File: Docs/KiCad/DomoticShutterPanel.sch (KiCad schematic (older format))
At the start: 32 parts, among them J1 Conn_01x02, J2 3.3V DC-DC Step-Down Power Mo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, J3 Conn_01x04, J4 BOOT OPTION, J5 UART COM, J6 Conn_01x04, J7 Conn_01x03, J9 Conn_01x03, K1 SRD-05VDC-SL-C, SW1 SW_Push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

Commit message: Updated 3D model to Crossed layout
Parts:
- added R? (x2): 8.2k, symbol CustomLibraries_Device:R
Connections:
- wire segments 144 -> 154
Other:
- note added: "ESP-WROOM-02"
- note added: "I2C PULLUP RESISTOR"
- note removed: "ESP-13e"
- moved on the sheet: J3, J?
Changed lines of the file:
@@
 Wire Wire Line
 	2400 1200 2950 1200
-Text Notes 8750 2200 0    50   ~ 0
+Text Notes 8350 2550 0    50   ~ 0
 LCD 16x2 I2C
 $Comp
 L CustomLibraries_connectors:Conn_01x04 J3
 U 1 1 5EA32128
-P 9350 2500
-F 0 "J3" H 9430 2492 50  0000 L CNN
-F 1 "Conn_01x04" H 9430 2401 50  0000 L CNN
-F 2 "Connector_PinHeader_2.54mm:PinHeader_1x04_P2.54mm_Vertical" H 9350 2500 50  0001 C CNN
-F 3 "~" H 9350 2500 50  0001 C CNN
-	1    9350 2500
-	1    0    0    -1
-$EndComp
-Wire Wire Line
-	9150 2400 9050 2400
-Wire Wire Line
-	9150 2500 8900 2500
-Wire Wire Line
-	9150 2600 8900 2600
-Wire Wire Line
-	9150 2700 8900 2700
+P 8950 2850
+F 0 "J3" H 9030 2842 50  0000 L CNN
+F 1 "Conn_01x04" H 9030 2751 50  0000 L CNN
+F 2 "Connector_PinHeader_2.54mm:PinHeader_1x04_P2.54mm_Vertical" H 8950 2850 50  0001 C CNN
+F 3 "~" H 8950 2850 50  0001 C CNN
+	1    8950 2850
+	1    0    0    -1
+$EndComp
+Wire Wire Line
+	8750 2750 8650 2750
+Wire Wire Line
+	8750 2850 8500 2850
+Wire Wire Line
+	8750 2950 8500 2950
+Wire Wire Line
+	8750 3050 8500 3050
 $Comp
 L CustomLibraries_power:GND #PWR04
 U 1 1 5EA49EAB
-P 9050 2850
-F 0 "#PWR04" H 9050 2600 50  0001 C CNN
-F 1 "GND" H 9055 2677 50  0000 C CNN
-F 2 "" H 9050 2850 50  0001 C CNN
-F 3 "" H 9050 2850 50  0001 C CNN
-	1    9050 2850
-	1    0    0    -1
-$EndComp
-Wire Wire Line
-	8900 2500 8900 2450
-Text Label 8950 2700 0    39   ~ 0
+P 8650 3200
+F 0 "#PWR04" H 8650 2950 50  0001 C CNN
+F 1 "GND" H 8655 3027 50  0000 C CNN
+F 2 "" H 8650 3200 50  0001 C CNN
+F 3 "" H 8650 3200 50  0001 C CNN
+	1    8650 3200
+	1    0    0    -1
+$EndComp
+Wire Wire Line
+	8500 2850 8500 2800
+Text Label 8550 3050 0    39   ~ 0
 I2C_SCL
 Wire Notes Line
-	8700 2100 9900 2100
-Wire Notes Line
-	9900 3100 8700 3100
-Wire Notes Line
-	9900 2100 9900 3100
-Wire Notes Line
-	8700 2100 8700 3100
+	8300 2450 9500 2450
+Wire Notes Line
+	9500 3450 8300 3450
+Wire Notes Line
+	9500 2450 9500 3450
+Wire Notes Line
+	8300 2450 8300 3450
 $Comp
 L CustomLibraries_SRD-05VDC-SL-C:SRD-05VDC-SL-C K1
@@
 L CustomLibraries_power:+5V #PWR0101
 U 1 1 5EB0B1CD
-P 8900 2450
-F 0 "#PWR0101" H 8900 2300 50  0001 C CNN
-F 1 "+5V" H 8915 2623 50  0000 C CNN
-F 2 "" H 8900 2450 50  0001 C CNN
-F 3 "" H 8900 2450 50  0001 C CNN
-	1    8900 2450
-	1    0    0    -1
-$EndComp
-Wire Wire Line
-	9050 2400 9050 2850
+P 8500 2800
+F 0 "#PWR0101" H 8500 2650 50  0001 C CNN
+F 1 "+5V" H 8515 2973 50  0000 C CNN
+F 2 "" H 8500 2800 50  0001 C CNN
+F 3 "" H 8500 2800 50  0001 C CNN
+	1    8500 2800
+	1    0    0    -1
+$EndComp
+Wire Wire Line
+	8650 2750 8650 3200
 $Comp
 L CustomLibraries_power:+5V #PWR0102
@@
 	1    0    0    -1
 $EndComp
-Text Notes 5150 4050 0    60   ~ 0
-ESP-13e
+Text Notes 4300 4050 0    60   ~ 0
+ESP-WROOM-02
 Wire Notes Line
 	3950 6850 3950 3900
@@
 Text Label 3050 6650 3    60   ~ 0
 A7
-Wire Notes Line
-	1875 4100 3050 4100
 Text Label 3600 5450 0    60   ~ 0
 A3
@@
 Wire Wire Line
 	5900 5800 6050 5800
-Text Label 8950 2600 0    39   ~ 0
+Text Label 8550 2950 0    39   ~ 0
 I2C_SDA
 Wire Wire Line
@@
 L CustomLibraries_connectors:Conn_01x03 J?
 U 1 1 5F3D7AAB
-P 9250 1100
-F 0 "J?" H 9330 1142 50  0000 L CNN
-F 1 "Conn_01x03" H 9330 1051 50  0000 L CNN
-F 2 "Connector_PinHeader_2.54mm:PinHeader_1x03_P2.54mm_Vertical" H 9250 1100 50  0001 C CNN
-F 3 "~" H 9250 1100 50  0001 C CNN
-	1    9250 1100
-	1    0    0    -1
-$EndComp
-Wire Notes Line
-	8750 1550 9900 1550
-Wire Notes Line
-	9900 1550 9900 600
-Wire Notes Line
-	9900 600  8750 600
-Wire Notes Line
-	8750 600  8750 1550
-Text Notes 8800 700  0    39   ~ 0
+P 8950 2050
+F 0 "J?" H 9030 2092 50  0000 L CNN
+F 1 "Conn_01x03" H 9030 2001 50  0000 L CNN
+F 2 "Connector_PinHeader_2.54mm:PinHeader_1x03_P2.54mm_Vertical" H 8950 2050 50  0001 C CNN
+F 3 "~" H 8950 2050 50  0001 C CNN
+	1    8950 2050
+	1    0    0    -1
+$EndComp
+Text Notes 8350 1700 0    39   ~ 0
 Lamp button
 Wire Wire Line
@@
 Wire Wire Line
 	8850 4600 8850 4500
+$Comp
+L CustomLibraries_power:+3V3 #PWR?
+U 1 1 5F493D6E
+P 10000 2700
+F 0 "#PWR?" H 10000 2550 50  0001 C CNN
+F 1 "+3V3" H 10015 2873 50  0000 C CNN
+F 2 "" H 10000 2700 50  0001 C CNN
+F 3 "" H 10000 2700 50  0001 C CNN
+	1    10000 2700
+	1    0    0    -1
+$EndComp
+Text Label 10150 3200 0    39   ~ 0
+I2C_SCL
+Text Label 10150 3300 0    39   ~ 0
+I2C_SDA
+Text Notes 9700 2450 0    39   ~ 0
+I2C PULLUP RESISTOR
+Wire Notes Line
+	8300 2400 9500 2400
+Wire Notes Line
+	8300 2400 8300 1600
+Wire Notes Line
+	8300 1600 9500 1600
+Wire Notes Line
+	9500 1600 9500 2400
+$Comp
+L CustomLibraries_Device:R R?
+U 1 1 5F4B85F8
+P 10100 2950
+F 0 "R?" H 10170 2996 50  0000 L CNN
+F 1 "8.2k" H 10170 2905 50  0000 L CNN
+F 2 "" V 10030 2950 50  0001 C CNN
+F 3 "~" H 10100 2950 50  0001 C CNN
+	1    10100 2950
+	1    0    0    -1
+$EndComp
+$Comp
+L CustomLibraries_Device:R R?
+U 1 1 5F4B940D
+P 9900 2950
+F 0 "R?" H 9700 3000 50  0000 L CNN
+F 1 "8.2k" H 9650 2900 50  0000 L CNN
+F 2 "" V 9830 2950 50  0001 C CNN
+F 3 "~" H 9900 2950 50  0001 C CNN
+	1    9900 2950
+	1    0    0    -1
+$EndComp
+Wire Notes Line
+	9600 3450 10450 3450
+Wire Notes Line
+	9600 2300 10450 2300
+Wire Notes Line
+	10450 2300 10450 3450
+Wire Notes Line
+	9600 2300 9600 3450
+Wire Wire Line
+	9900 3100 9900 3200
+Connection ~ 9900 3200
+Wire Wire Line
+	9900 3200 10400 3200
+Wire Wire Line
+	10100 3100 10100 3300
+Connection ~ 10100 3300
+Wire Wire Line
+	10100 3300 10400 3300
+Wire Wire Line
+	9900 2800 9900 2700
+Wire Wire Line
+	9900 2700 10000 2700
+Wire Wire Line
+	10100 2800 10100 2700
+Wire Wire Line
+	10100 2700 10000 2700
+Connection ~ 10000 2700
+Wire Wire Line
+	9700 3200 9900 3200
+Wire Wire Line
+	9700 3300 10100 3300
 $EndSCHEMATC

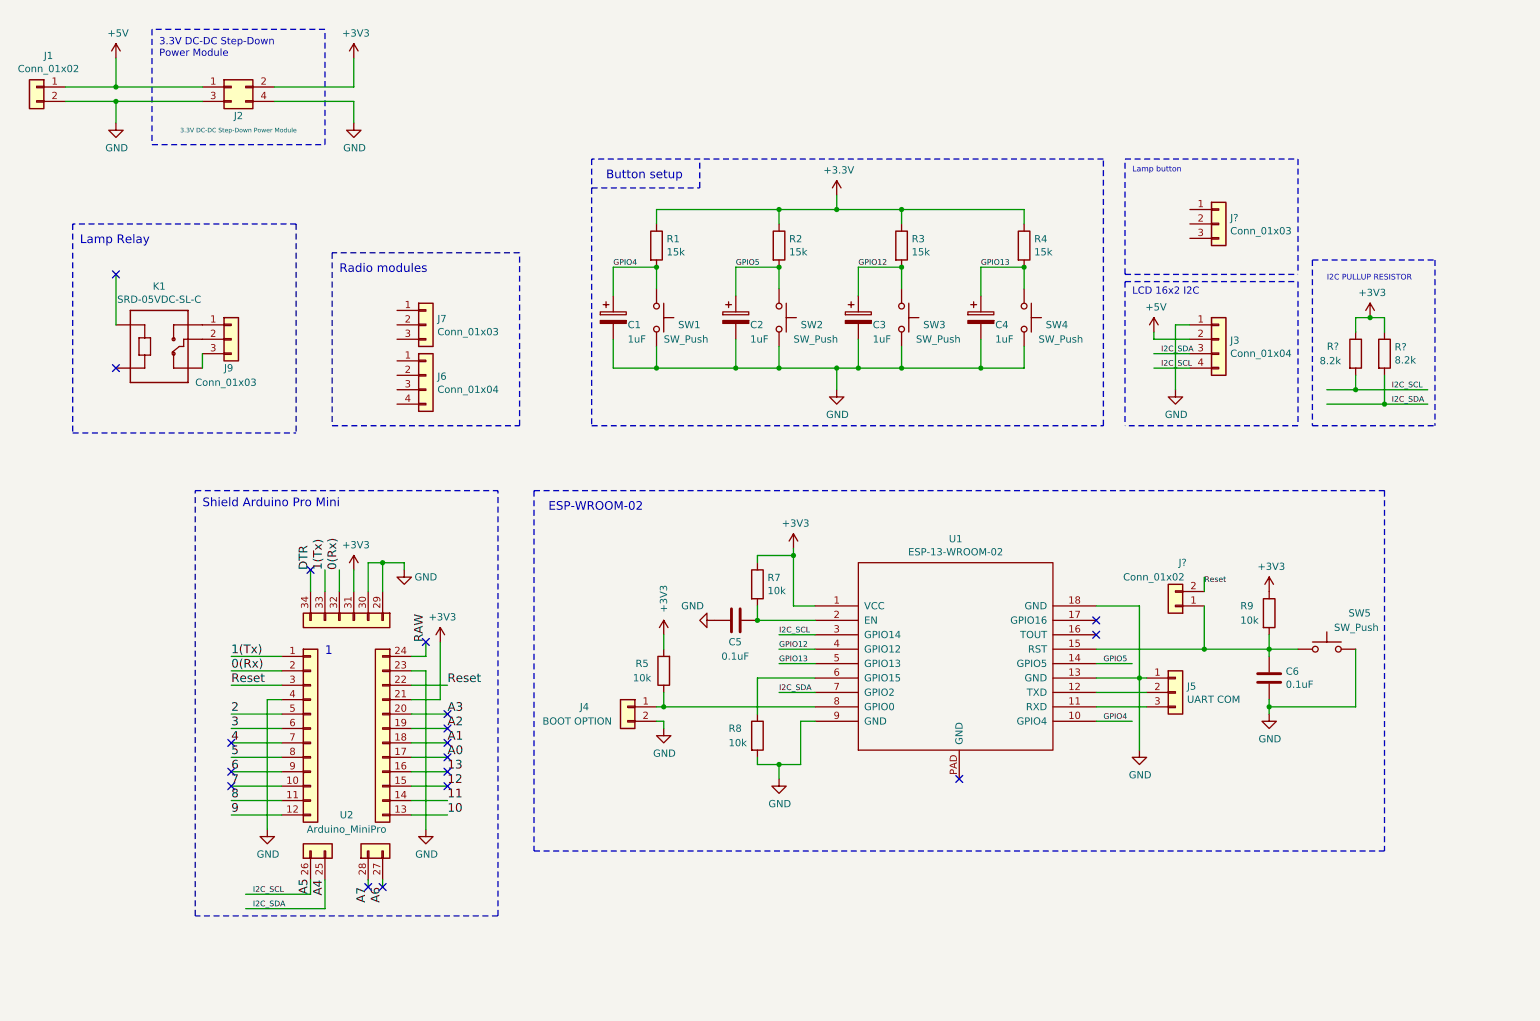
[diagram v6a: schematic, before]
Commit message: Changed text labels
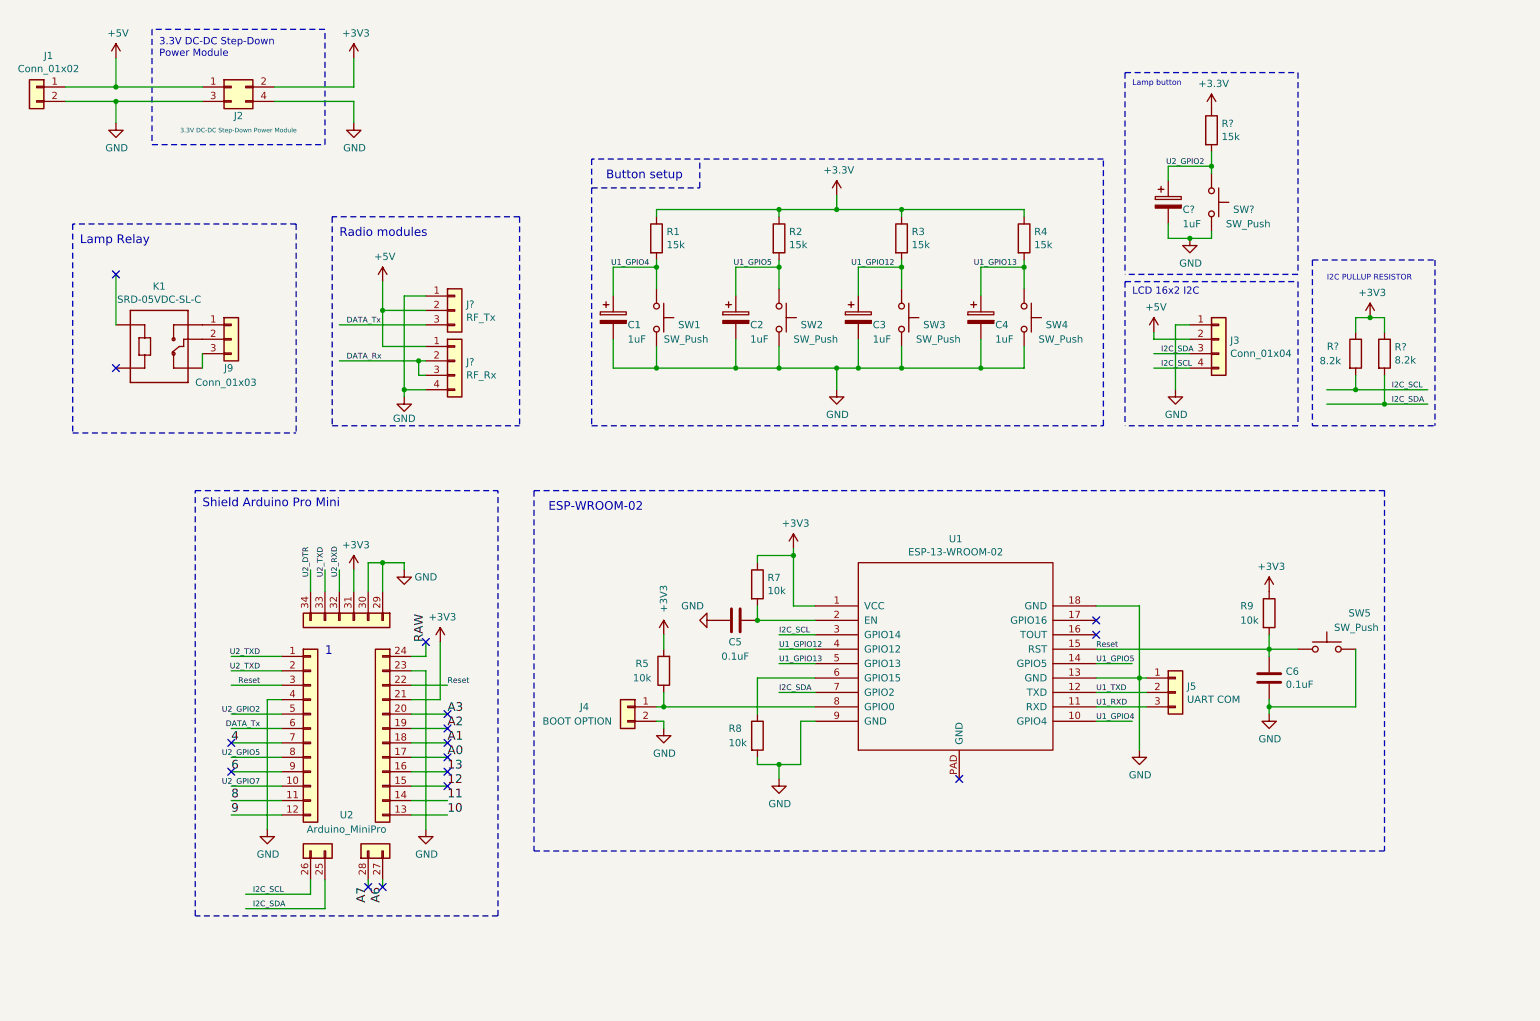
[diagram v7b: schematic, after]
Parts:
- removed J?: Conn_01x03, Connector_PinHeader_2.54mm:PinHeader_1x03_P2.54mm_Vertical, symbol CustomLibraries_connectors:Conn_01x03
- removed J?: Conn_01x02, symbol CustomLibraries_connectors:Conn_01x02
- added C?: 1uF, Capacitor_THT:C_Radial_D5.0mm_H5.0mm_P2.00mm, symbol CustomLibraries_Device:CP
- added R?: 15k, Resistor_THT:R_Axial_DIN0204_L3.6mm_D1.6mm_P1.90mm_Vertical, symbol CustomLibraries_Device:R
- added SW?: SW_Push, Custom_libraries:SW_PUSH_6mm, symbol CustomLibraries_Switch:SW_Push
- J?: renamed from J6; value Conn_01x04 -> RF_Rx
- J?: renamed from J7; value Conn_01x03 -> RF_Tx
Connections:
- net labels added: DATA_Rx, DATA_Tx, U1_GPIO12, U1_GPIO13, U1_GPIO4, U1_GPIO5, U1_RXD, U1_TXD, U2_DTR, U2_GPIO2, U2_GPIO5, U2_GPIO7, U2_RXD, U2_TXD
- net labels removed: 0(Rx), 1(Tx), 2, 3, 5, 7, A4, A5, DTR, GPIO12, GPIO13, GPIO4, GPIO5
- wire segments 154 -> 176
- no-connect marks 18 -> 16
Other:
- moved on the sheet: J?, R1, R2, R3, R4

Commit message: Added buzzer and 3d model updated
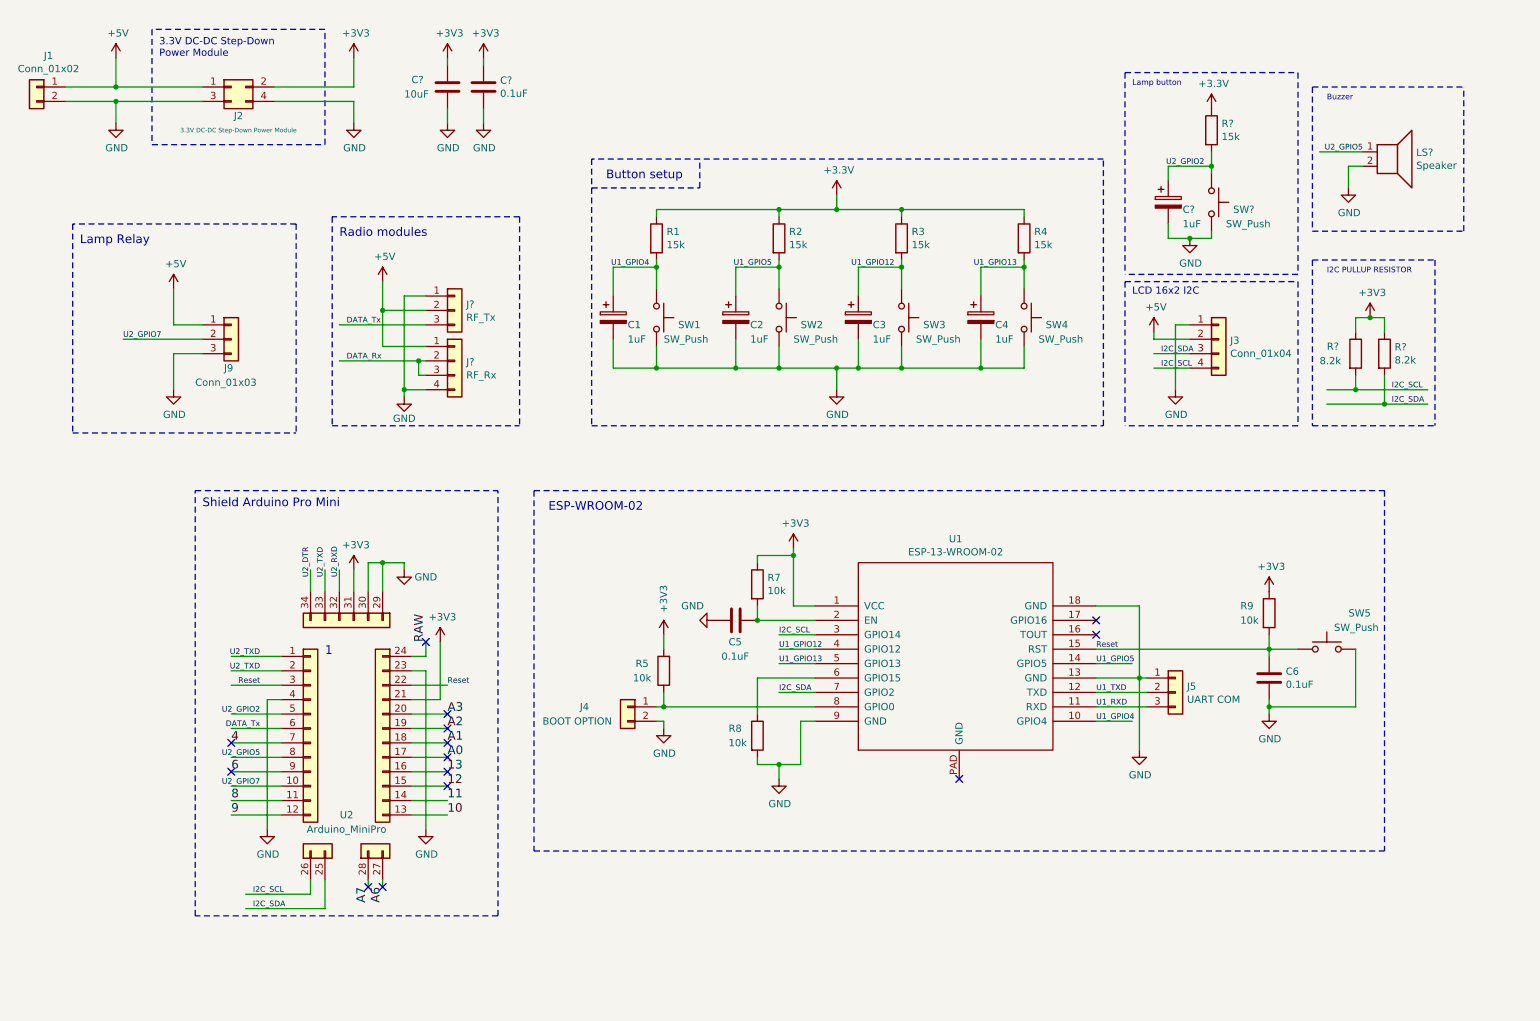
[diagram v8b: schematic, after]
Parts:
- removed K1: SRD-05VDC-SL-C, Custom_libraries:RELAY_SRD-05VDC-SL-C, symbol CustomLibraries_SRD-05VDC-SL-C:SRD-05VDC-SL-C
- added C?: 10uF, symbol CustomLibraries_Device:C
- added C?: 0.1uF, symbol CustomLibraries_Device:C
- added LS?: Speaker, symbol CustomLibraries_Device:Speaker
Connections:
- wire segments 176 -> 186
- no-connect marks 16 -> 14
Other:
- note added: "Buzzer"
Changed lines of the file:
@@
 Sheet 1 1
 Title "Roller Shutter Controller Panel"
-Date "2020-04-24"
+Date "2020-08-30"
 Rev ""
 Comp ""
@@
 Wire Wire Line
 	6300 1950 6750 1950
-Wire Wire Line
-	1300 2400 1300 2750
-Wire Wire Line
-	1900 2950 1900 3050
-$Comp
-L CustomLibraries_connectors:Conn_01x03 J9
-U 1 1 5EACF56F
-P 2100 2850
-F 0 "J9" H 2050 2650 50  0000 L CNN
-F 1 "Conn_01x03" H 1850 2550 50  0000 L CNN
-F 2 "Connector_PinHeader_2.54mm:PinHeader_1x03_P2.54mm_Vertical" H 2100 2850 50  0001 C CNN
-F 3 "~" H 2100 2850 50  0001 C CNN
-	1    2100 2850
-	1    0    0    -1
-$EndComp
-Wire Notes Line
-	1000 3500 2550 3500
-Wire Notes Line
-	2550 2050 1000 2050
-Text Notes 1050 2200 0    60   ~ 0
-Lamp Relay
-Wire Notes Line
-	1000 2050 1000 3500
-Wire Notes Line
-	2550 2050 2550 3500
 $Comp
 L CustomLibraries_connectors:Conn_01x02 J1
@@
 Wire Notes Line
 	8300 2450 8300 3450
-$Comp
-L CustomLibraries_SRD-05VDC-SL-C:SRD-05VDC-SL-C K1
-U 1 1 5EACF577
-P 1600 2850
-F 0 "K1" H 1600 3217 50  0000 C CNN
-F 1 "SRD-05VDC-SL-C" H 1600 3126 50  0000 C CNN
-F 2 "Custom_libraries:RELAY_SRD-05VDC-SL-C" H 1600 2850 50  0001 L BNN
-F 3 "" H 1600 2850 50  0001 L BNN
-F 4 "IPC-7251" H 1600 2850 50  0001 L BNN "Campo4"
-	1    1600 2850
-	1    0    0    -1
-$EndComp
-NoConn ~ 1300 3050
-NoConn ~ 1300 2400
 $Comp
 L CustomLibraries_power:+5V #PWR0101
@@
 Text Label 10150 3300 0    39   ~ 0
 I2C_SDA
-Text Notes 9700 2450 0    39   ~ 0
+Text Notes 9700 2400 0    39   ~ 0
 I2C PULLUP RESISTOR
 $Comp
@@
 Text Label 2650 4500 1    39   ~ 0
 U2_DTR
+$Comp
+L CustomLibraries_Device:Speaker LS?
+U 1 1 5F4B04D1
+P 10150 1550
+F 0 "LS?" H 10320 1546 50  0000 L CNN
+F 1 "Speaker" H 10320 1455 50  0000 L CNN
+F 2 "" H 10150 1350 50  0001 C CNN
+F 3 "~" H 10140 1500 50  0001 C CNN
+	1    10150 1550
+	1    0    0    -1
+$EndComp
+Wire Wire Line
+	9950 1650 9850 1650
+Wire Wire Line
+	9850 1650 9850 1800
+Wire Wire Line
+	9950 1550 9650 1550
+Text Label 9950 1550 2    39   ~ 0
+U2_GPIO5
+$Comp
+L CustomLibraries_power:GND #PWR?
+U 1 1 5F4C460A
+P 9850 1800
+F 0 "#PWR?" H 9850 1550 50  0001 C CNN
+F 1 "GND" H 9855 1627 50  0000 C CNN
+F 2 "" H 9850 1800 50  0001 C CNN
+F 3 "" H 9850 1800 50  0001 C CNN
+	1    9850 1800
+	1    0    0    -1
+$EndComp
+Wire Notes Line
+	9600 1100 9600 2100
+Wire Notes Line
+	9600 2100 10650 2100
+Wire Notes Line
+	10650 2100 10650 1100
+Wire Notes Line
+	9600 1100 10650 1100
+Text Notes 9700 1200 0    39   ~ 0
+Buzzer
+Wire Wire Line
+	3600 900  3600 950
+$Comp
+L CustomLibraries_power:GND #PWR?
+U 1 1 5F4B3969
+P 3600 1350
+F 0 "#PWR?" H 3600 1100 50  0001 C CNN
+F 1 "GND" H 3605 1177 50  0000 C CNN
+F 2 "" H 3600 1350 50  0001 C CNN
+F 3 "" H 3600 1350 50  0001 C CNN
+	1    3600 1350
+	1    0    0    -1
+$EndComp
+$Comp
+L CustomLibraries_power:+3V3 #PWR?
+U 1 1 5F4B3972
+P 3600 900
+F 0 "#PWR?" H 3600 750 50  0001 C CNN
+F 1 "+3V3" H 3615 1073 50  0000 C CNN
+F 2 "" H 3600 900 50  0001 C CNN
+F 3 "" H 3600 900 50  0001 C CNN
+	1    3600 900
+	1    0    0    -1
+$EndComp
+$Comp
+L CustomLibraries_Device:C C?
+U 1 1 5F4D102B
+P 3600 1100
+F 0 "C?" H 3350 1150 50  0000 L CNN
+F 1 "10uF" H 3300 1050 50  0000 L CNN
+F 2 "" H 3638 950 50  0001 C CNN
+F 3 "~" H 3600 1100 50  0001 C CNN
+	1    3600 1100
+	1    0    0    -1
+$EndComp
+Wire Wire Line
+	3600 1250 3600 1350
+Wire Wire Line
+	3850 900  3850 950
+$Comp
+L CustomLibraries_power:GND #PWR?
+U 1 1 5F4DD2EB
+P 3850 1350
+F 0 "#PWR?" H 3850 1100 50  0001 C CNN
+F 1 "GND" H 3855 1177 50  0000 C CNN
+F 2 "" H 3850 1350 50  0001 C CNN
+F 3 "" H 3850 1350 50  0001 C CNN
+	1    3850 1350
+	1    0    0    -1
+$EndComp
+$Comp
+L CustomLibraries_power:+3V3 #PWR?
+U 1 1 5F4DD2F1
+P 3850 900
+F 0 "#PWR?" H 3850 750 50  0001 C CNN
+F 1 "+3V3" H 3865 1073 50  0000 C CNN
+F 2 "" H 3850 900 50  0001 C CNN
+F 3 "" H 3850 900 50  0001 C CNN
+	1    3850 900
+	1    0    0    -1
+$EndComp
+$Comp
+L CustomLibraries_Device:C C?
+U 1 1 5F4DD2F7
+P 3850 1100
+F 0 "C?" H 3965 1146 50  0000 L CNN
+F 1 "0.1uF" H 3965 1055 50  0000 L CNN
+F 2 "" H 3888 950 50  0001 C CNN
+F 3 "~" H 3850 1100 50  0001 C CNN
+	1    3850 1100
+	1    0    0    -1
+$EndComp
+Wire Wire Line
+	3850 1250 3850 1350
+Wire Notes Line
+	2550 2050 2550 3500
+Wire Notes Line
+	1000 2050 1000 3500
+Text Notes 1050 2200 0    60   ~ 0
+Lamp Relay
+Wire Notes Line
+	2550 2050 1000 2050
+$Comp
+L CustomLibraries_connectors:Conn_01x03 J9
+U 1 1 5EACF56F
+P 2100 2850
+F 0 "J9" H 2050 2650 50  0000 L CNN
+F 1 "Conn_01x03" H 1850 2550 50  0000 L CNN
+F 2 "Connector_PinHeader_2.54mm:PinHeader_1x03_P2.54mm_Vertical" H 2100 2850 50  0001 C CNN
+F 3 "~" H 2100 2850 50  0001 C CNN
+	1    2100 2850
+	1    0    0    -1
+$EndComp
+Wire Notes Line
+	1000 3500 2550 3500
+$Comp
+L CustomLibraries_power:GND #PWR?
+U 1 1 5F4E22CF
+P 1700 3200
+F 0 "#PWR?" H 1700 2950 50  0001 C CNN
+F 1 "GND" H 1705 3027 50  0000 C CNN
+F 2 "" H 1700 3200 50  0001 C CNN
+F 3 "" H 1700 3200 50  0001 C CNN
+	1    1700 3200
+	1    0    0    -1
+$EndComp
+Wire Wire Line
+	1700 2950 1700 3200
+Wire Wire Line
+	1700 2950 1900 2950
+Wire Wire Line
+	1900 2750 1700 2750
+Wire Wire Line
+	1700 2750 1700 2500
+$Comp
+L CustomLibraries_power:+5V #PWR?
+U 1 1 5F50527A
+P 1700 2500
+F 0 "#PWR?" H 1700 2350 50  0001 C CNN
+F 1 "+5V" H 1715 2673 50  0000 C CNN
+F 2 "" H 1700 2500 50  0001 C CNN
+F 3 "" H 1700 2500 50  0001 C CNN
+	1    1700 2500
+	1    0    0    -1
+$EndComp
+Wire Wire Line
+	1900 2850 1350 2850
+Text Label 1350 2850 0    39   ~ 0
+U2_GPIO7
 $EndSCHEMATC
